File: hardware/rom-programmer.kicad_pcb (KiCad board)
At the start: 2 copper layers, 130 x 75 mm, 64 parts, among them U1 74HC595, U2 74HC595, U3 28C256, U4 74HC00

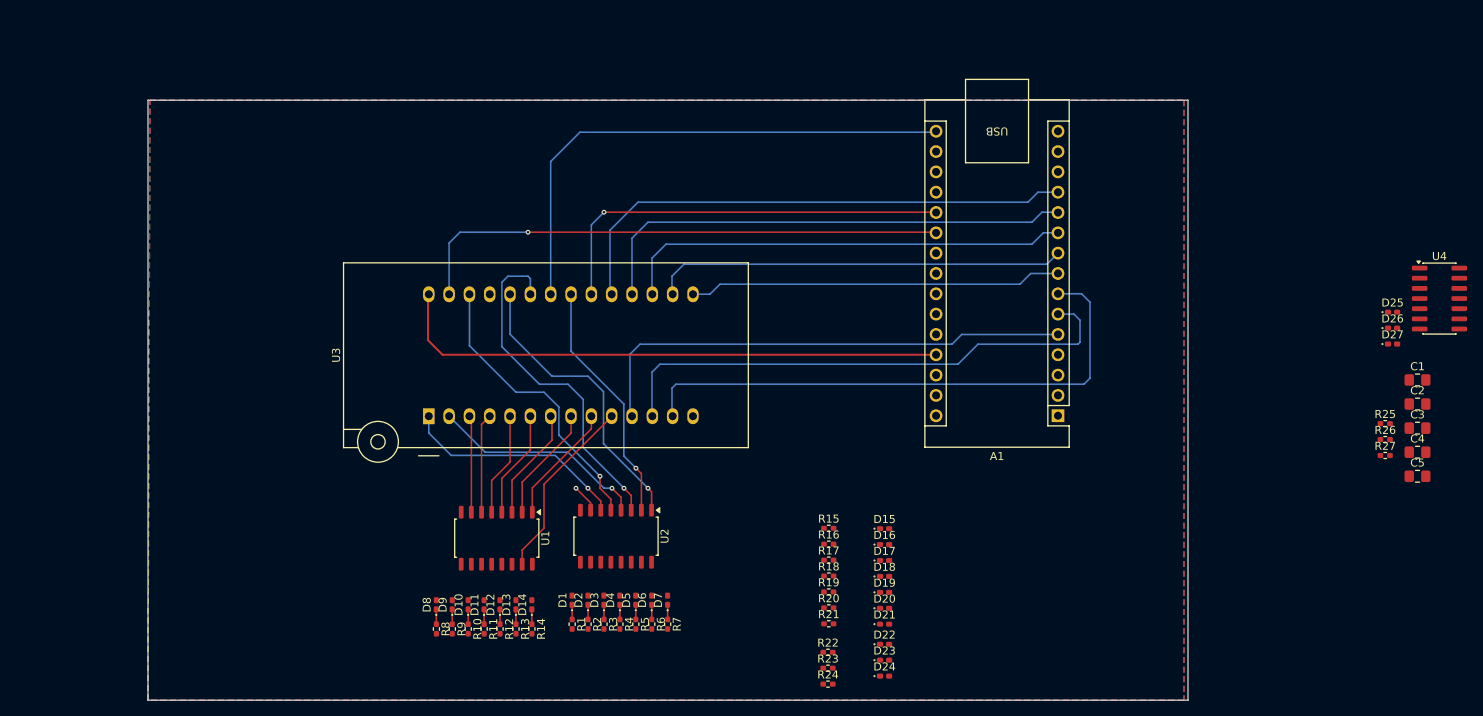
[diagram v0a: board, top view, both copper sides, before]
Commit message: Erase and timing seems to work correctly and reliably now
Co-authored-by: Copilot <copilot@github.com>
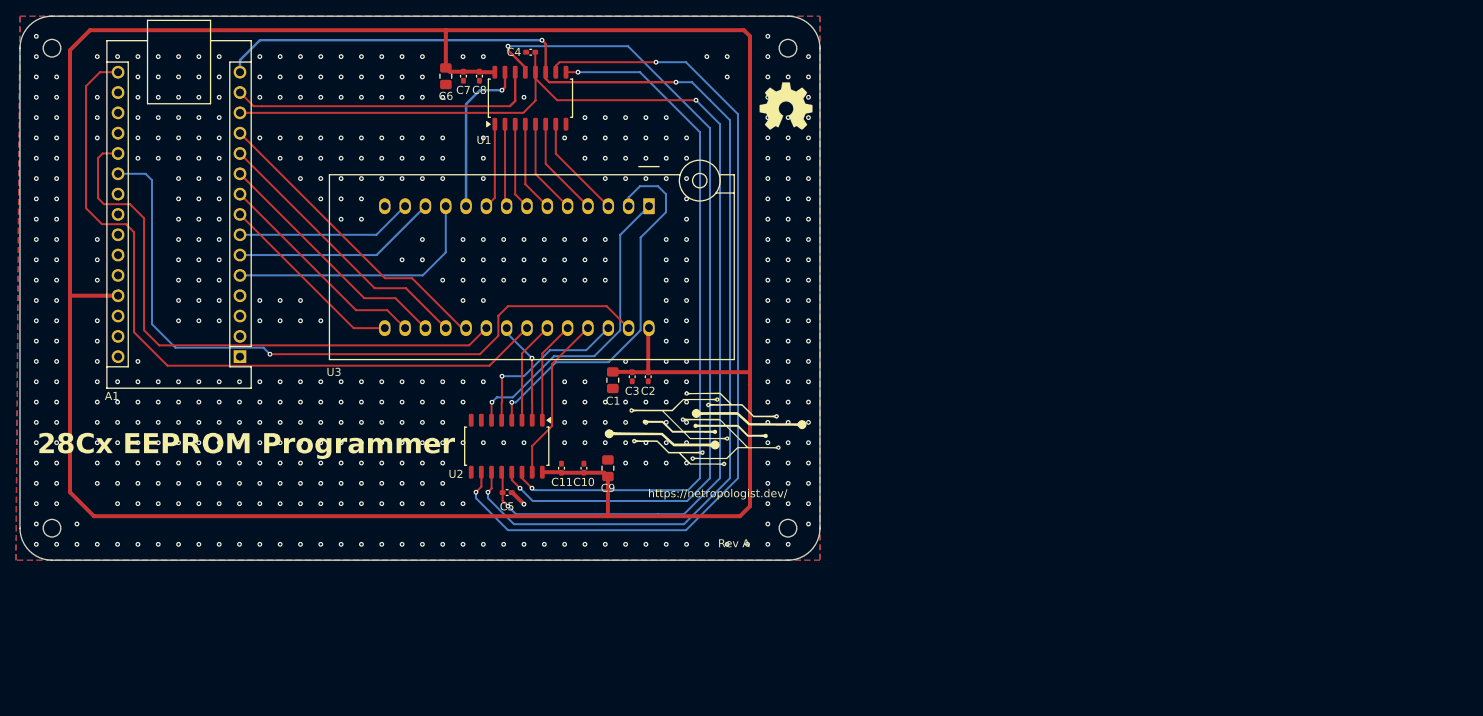
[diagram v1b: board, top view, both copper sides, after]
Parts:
- removed D1, D2, D3, D4, D5, D6, D7: RED, Diode_SMD:D_0402_1005Metric_Pad0.77x0.64mm_HandSolder
- removed D10, D11, D12, D13, D14, D8, D9: GREEN, Diode_SMD:D_0402_1005Metric_Pad0.77x0.64mm_HandSolder
- removed D15, D16, D17, D18, D19, D20, D21, D22, D23, D24: WHITE, Diode_SMD:D_0402_1005Metric_Pad0.77x0.64mm_HandSolder
- removed D25, D26, D27: BLUE, Diode_SMD:D_0402_1005Metric_Pad0.77x0.64mm_HandSolder
- removed R1, R10, R11, R12, R13, R14, R15, R16, R17, R18, R19, R2, R20, R21, R22, R23, R24, R25, R26, R27, R3, R4, R5, R6, R7, R8, R9: 2k2, Resistor_SMD:R_0402_1005Metric_Pad0.72x0.64mm_HandSolder
- removed U4: 74HC00, Package_SO:SO-14_3.9x8.65mm_P1.27mm
- added C10: 0.1uF, Capacitor_SMD:C_0402_1005Metric_Pad0.74x0.62mm_HandSolder, F.Cu at (160.5, 119.0)
- added C11: 0.1uF, Capacitor_SMD:C_0402_1005Metric_Pad0.74x0.62mm_HandSolder, F.Cu at (157.7, 119.0)
- added C6: 1uF, Capacitor_SMD:C_0805_2012Metric_Pad1.18x1.45mm_HandSolder, F.Cu at (143.2, 70.0)
- added C7: 0.1uF, Capacitor_SMD:C_0402_1005Metric_Pad0.74x0.62mm_HandSolder, F.Cu at (145.4, 70.0)
- added C8: 0.1uF, Capacitor_SMD:C_0402_1005Metric_Pad0.74x0.62mm_HandSolder, F.Cu at (147.4, 70.0)
- added C9: 1uF, Capacitor_SMD:C_0805_2012Metric_Pad1.18x1.45mm_HandSolder, F.Cu at (163.5, 119.0)
- added G***: LOGO, tne logo tiny, F.Cu at (175.8, 114.0)
- added H1: MountingHole, MountingHole:MountingHole_2.2mm_M2, F.Cu at (94.0, 66.5)
- added H2: MountingHole, MountingHole:MountingHole_2.2mm_M2, F.Cu at (186.0, 66.5)
- added H3: MountingHole, MountingHole:MountingHole_2.2mm_M2, F.Cu at (186.0, 126.5)
- added H4: MountingHole, MountingHole:MountingHole_2.2mm_M2, F.Cu at (94.0, 126.5)
- added REF**: OSHW-Symbol_6.7x6mm_SilkScreen, Symbol:OSHW-Symbol_6.7x6mm_SilkScreen, F.Cu at (185.8, 73.8)
- C1: value 100pF -> 1uF
- C2, C3, C4, C5: value 100pF -> 0.1uF; footprint Capacitor_SMD:C_0805_2012Metric_Pad1.18x1.45mm_HandSolder -> Capacitor_SMD:C_0402_1005Metric_Pad0.74x0.62mm_HandSolder
- moved C4 121.6 mm to (153.8, 67.0), turned to 180 degrees
- moved C5 113.8 mm to (150.9, 122.0)
- moved A1 102.5 mm to (117.5, 105.1)
- moved C1 100.6 mm to (164.1, 108.0), turned to -90 degrees
- moved C3 98.4 mm to (166.5, 107.6), turned to -90 degrees
- moved C2 96.2 mm to (168.5, 107.6), turned to -90 degrees
- moved U1 55.2 mm to (153.8, 72.8), turned to 90 degrees
- moved U3 38.0 mm to (168.6, 86.2), turned to -90 degrees
- moved U2 17.7 mm to (150.8, 116.2)
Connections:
- A1 pad 28: /~{RST} -> unconnected-(A1-~{RESET}-Pad28)
- A1 pad 3: /~{RST} -> unconnected-(A1-~{RESET}-Pad3)
- C4 pad 1: +5V -> /RCLK
- C5 pad 1: +5V -> /RCLK
- U1 pad 14: /SER -> /SRDATA
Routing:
- net +5V: track 70.0 -> 340.4 mm
- net /SRCLK: track 0.00 -> 152.6 mm, vias 0 -> 3
- net /RCLK: track 0.00 -> 147.5 mm, vias 0 -> 2
- net /CRCLR: track 0.00 -> 112.6 mm, vias 0 -> 2
- net /~{SER_OE}: track 0.00 -> 105.4 mm, vias 0 -> 2
- net /SERO: track 0.00 -> 87.3 mm, vias 0 -> 2
- net /D2: track 70.2 -> 22.1 mm
- net /D1: track 66.4 -> 25.7 mm
- net /SRDATA: track 0.00 -> 39.0 mm
- net /A11: track 43.2 -> 12.8 mm, vias 1 -> 0
- net /D0: track 62.4 -> 32.7 mm
- net /D7: track 66.1 -> 38.4 mm
- net /D6: track 61.6 -> 34.8 mm
- net /~{ROM_OE}: track 66.3 -> 92.5 mm
- net /D5: track 56.6 -> 31.2 mm
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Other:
- board size 130 x 75 mm -> 100 x 68 mm
- board text added: "28Cx EEPROM Programmer"
- board text added: "Rev A"
- board text added: "https://netropologist.dev/"
